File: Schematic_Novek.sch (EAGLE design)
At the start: 28 parts, among them IC1 STM32F10XCXT6, U1 BQ21040

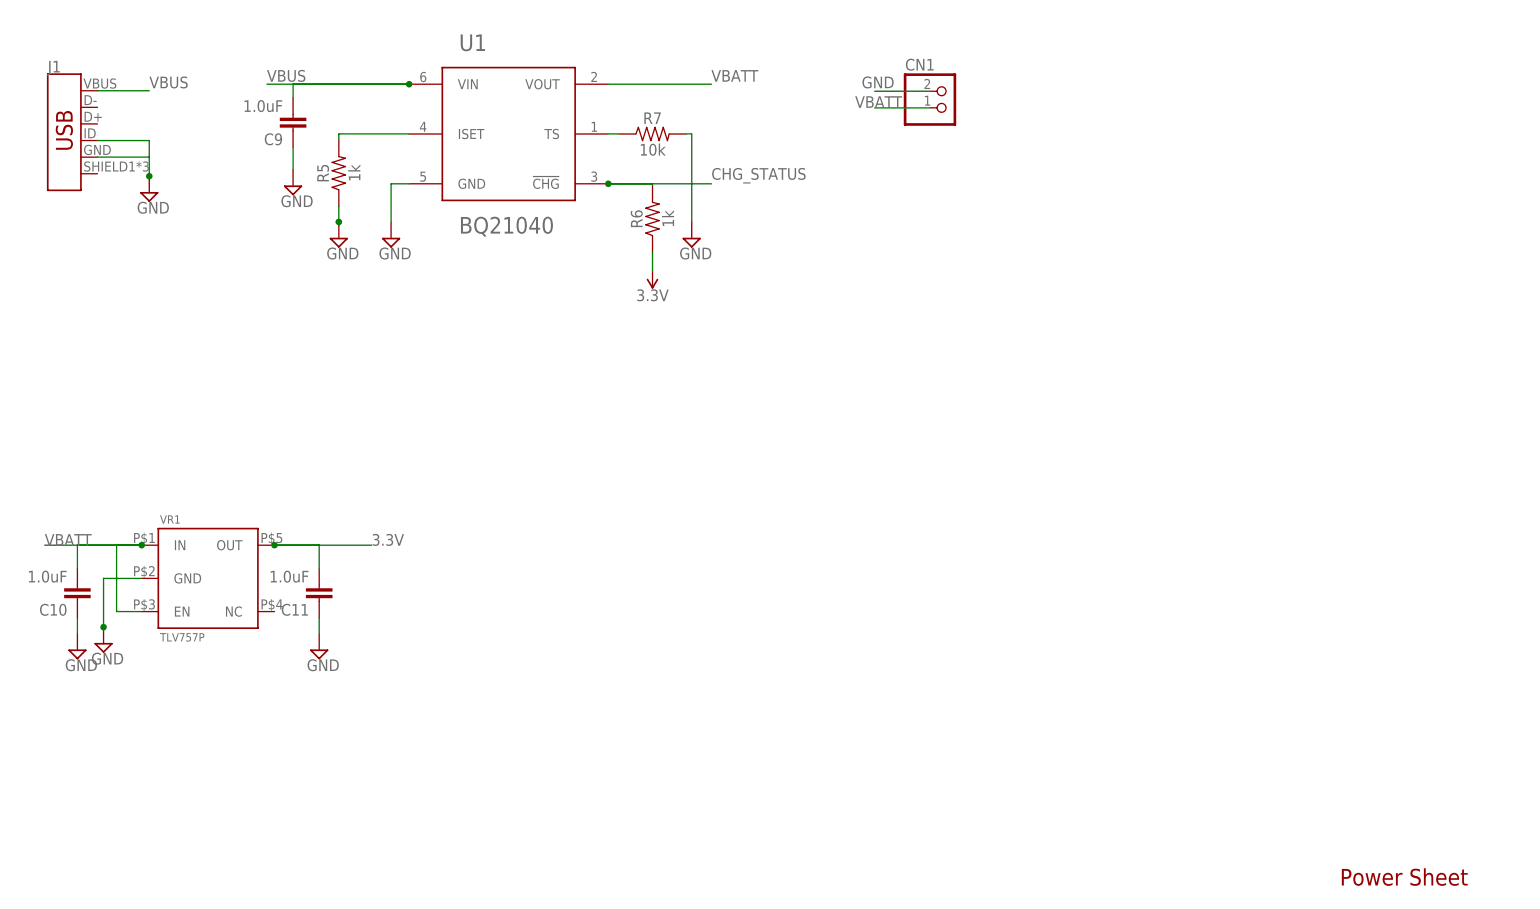
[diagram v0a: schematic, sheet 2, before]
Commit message: Adds max17048 fuel gauge
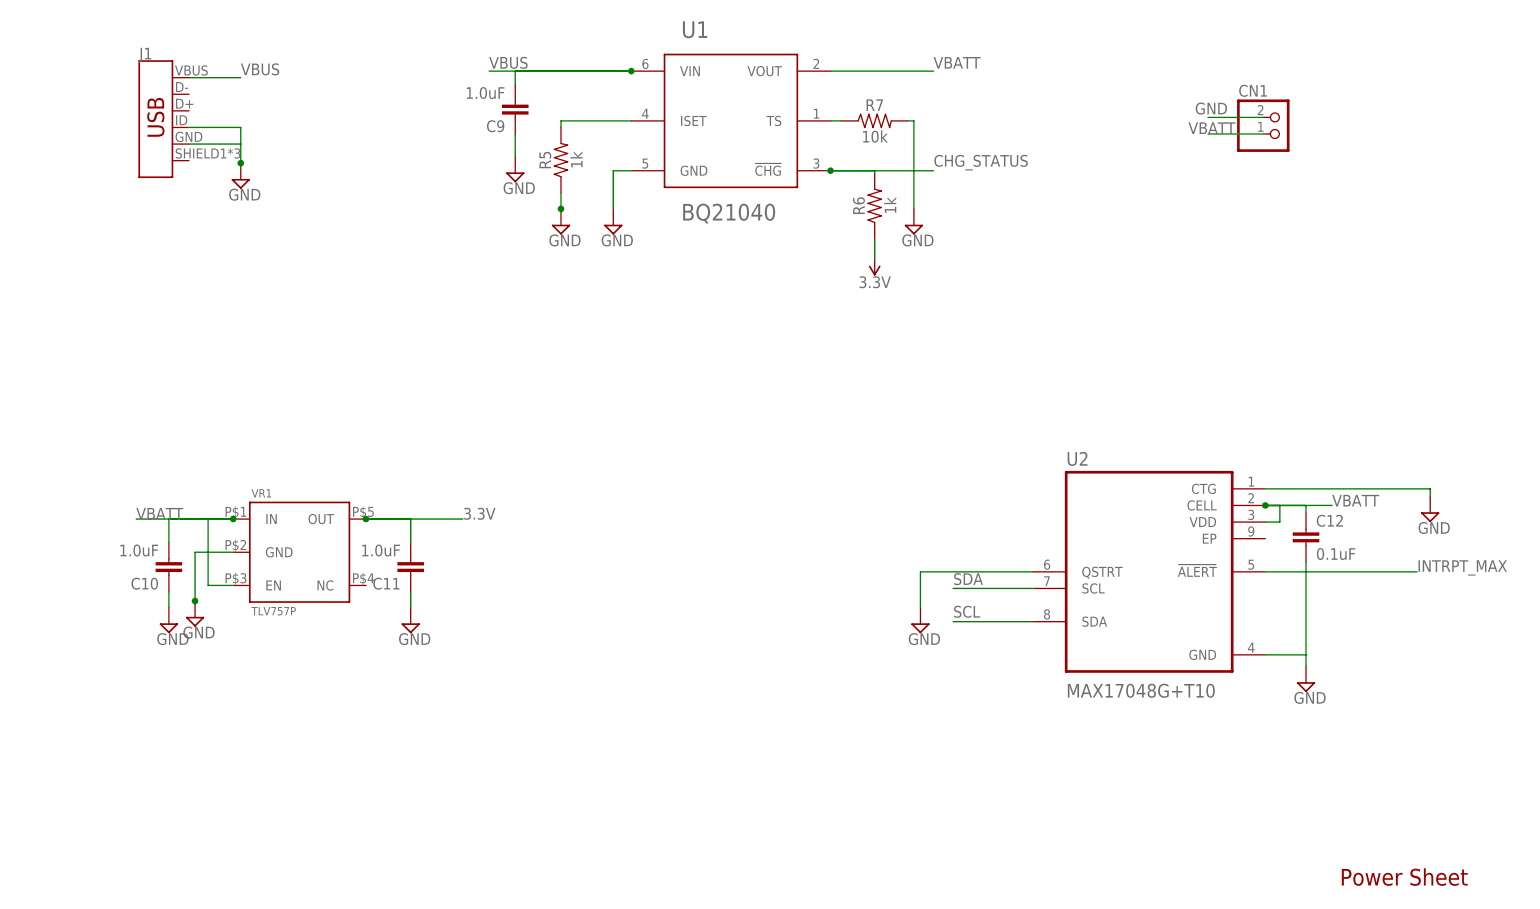
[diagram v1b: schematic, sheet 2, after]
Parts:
- added C12: 0.1uF, SparkFun-Capacitors:0.1UF-0603-25V-(+80/-20%)
- added U2: MAX17048G+T10, MAX17048G_T10:MAX17048G+T10
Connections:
- new net INTRPT_MAX: U2.!ALERT
- new net SCL: U2.SDA
- new net SDA: U2.SCL
- net GND: now also C12.2, U2.CTG, U2.GND, U2.QSTRT
- net VBATT: now also C12.1, U2.CELL, U2.VDD
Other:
- moved on the sheet: C10, C11, C9, CN1, J1, R5, R6, R7, U1, VR1

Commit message: Adds new sensor sheet
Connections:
- net CHG_STATUS: now also IC1PORTA_H.PA15
- net INTRPT_MAX: now also IC1PORTB_L.PB4
- net SCL: now also IC1PORTB_L.PB6
- net SDA: now also IC1PORTB_L.PB7
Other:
- note added: "Sensors + Transducers"
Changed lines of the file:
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@@
 <part name="SUPPLY25" library="supply2" deviceset="GND" device=""/>
 <part name="SUPPLY26" library="supply2" deviceset="GND" device=""/>
+<part name="FRAME3" library="frames" deviceset="A4L-LOC" device=""/>
 </parts>
 <sheets>
@@
 </segment>
 </net>
+<net name="SDA" class="0">
+<segment>
+<pinref part="IC1" gate="PORTB_L" pin="PB7"/>
+<wire x1="137.16" y1="114.3" x2="143" y2="114.3" width="0.1524" layer="91"/>
+<label x="143" y="115" size="1.778" layer="95"/>
+</segment>
+</net>
+<net name="SCL" class="0">
+<segment>
+<pinref part="IC1" gate="PORTB_L" pin="PB6"/>
+<wire x1="137.16" y1="116.84" x2="143" y2="116.84" width="0.1524" layer="91"/>
+<label x="143" y="117" size="1.778" layer="95"/>
+</segment>
+</net>
+<net name="INTRPT_MAX" class="0">
+<segment>
+<pinref part="IC1" gate="PORTB_L" pin="PB4"/>
+<wire x1="137.16" y1="121.92" x2="143" y2="121.92" width="0.1524" layer="91"/>
+<label x="143" y="122" size="1.778" layer="95"/>
+</segment>
+</net>
+<net name="CHG_STATUS" class="0">
+<segment>
+<pinref part="IC1" gate="PORTA_H" pin="PA15"/>
+<wire x1="101.6" y1="88.9" x2="91" y2="88.9" width="0.1524" layer="91"/>
+<label x="84" y="89" size="1.778" layer="95"/>
+</segment>
+</net>
 </nets>
 </sheet>
@@
 </nets>
 </sheet>
+<sheet>
+<plain>
+<text x="217.17" y="20" size="2.54" layer="94">Sensors + Transducers</text>
+</plain>
+<instances>
+<instance part="FRAME3" gate="G$1" x="0" y="0" smashed="yes">
+<attribute name="DRAWING_NAME" x="217.17" y="15.24" size="2.54" layer="94"/>
+<attribute name="LAST_DATE_TIME" x="217.17" y="10.16" size="2.286" layer="94"/>
+<attribute name="SHEET" x="230.505" y="5.08" size="2.54" layer="94"/>
+</instance>
+</instances>
+<busses>
+</busses>
+<nets>
+</nets>
+</sheet>

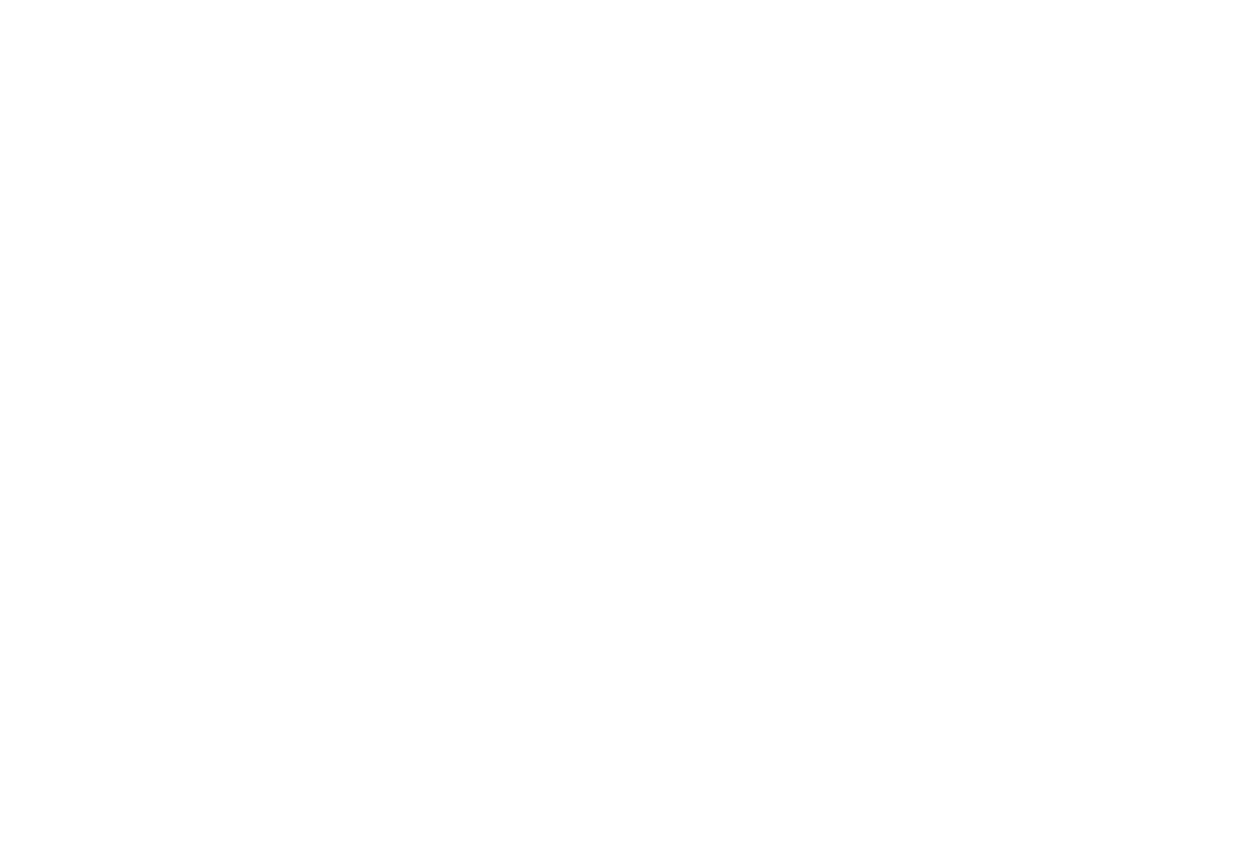
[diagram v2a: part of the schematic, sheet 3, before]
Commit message: Adds pressure gauge
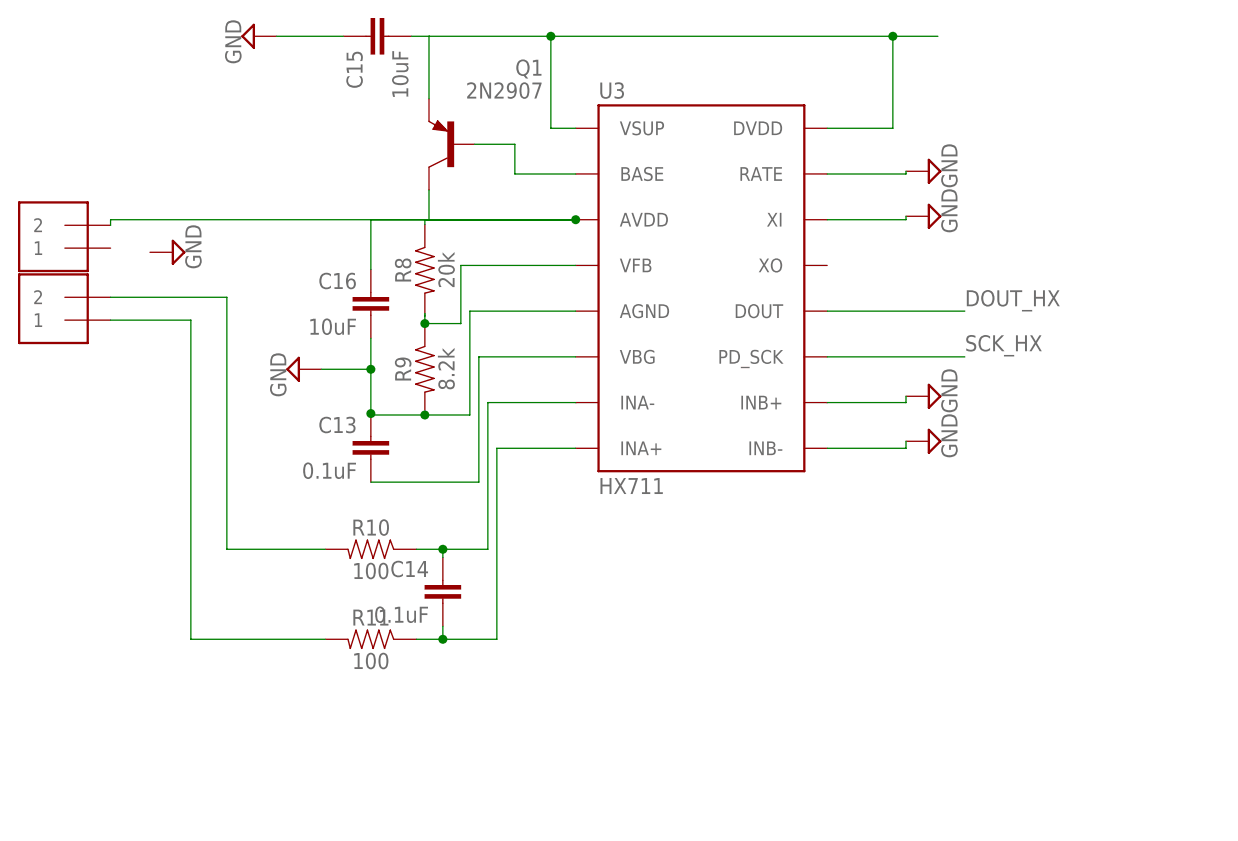
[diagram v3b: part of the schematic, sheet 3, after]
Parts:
- added C13, C14: 0.1uF, SparkFun-Capacitors:0.1UF-0603-25V-5%
- added C15, C16: 10uF, SparkFun-Capacitors:10UF-0603-6.3V-20%
- added J2, J3: 1X2-3.5MM, adafruit:1X2-3.5MM
- added Q1: 2N2907, adafruit:2N2907
- added R10, R11: 100, SparkFun-Resistors:100OHM-0603-1/10W-1%
- added R8: 20k, SparkFun-Resistors:20KOHM-0603-1/10W-1%
- added R9: 8.2k, SparkFun-Resistors:8.2KOHM-0603-1/10W-5%
- added U3: HX711, SparkFun-IC-Conversion:HX711
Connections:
- new net DOUT_HX: U3.DOUT
- new net N$10: C13.2, U3.VBG
- new net N$11: R8.2, R9.1, U3.VFB
- new net N$12: C14.1, R10.1, U3.INA-
- new net N$13: C14.2, R11.1, U3.INA+
- new net N$5: Q1.B, U3.BASE
- new net N$6: C15.2, Q1.E, U3.DVDD, U3.VSUP
- new net N$7: C16.1, J2.2, Q1.C, R8.1, U3.AVDD
- new net N$8: J3.2, R10.2
- new net N$9: J3.1, R11.2
- new net SCK_HX: U3.PD_SCK
- net GND: now also C13.1, C15.1, C16.2, R9.2, U3.AGND, U3.INB+, U3.INB-, U3.RATE, U3.XI

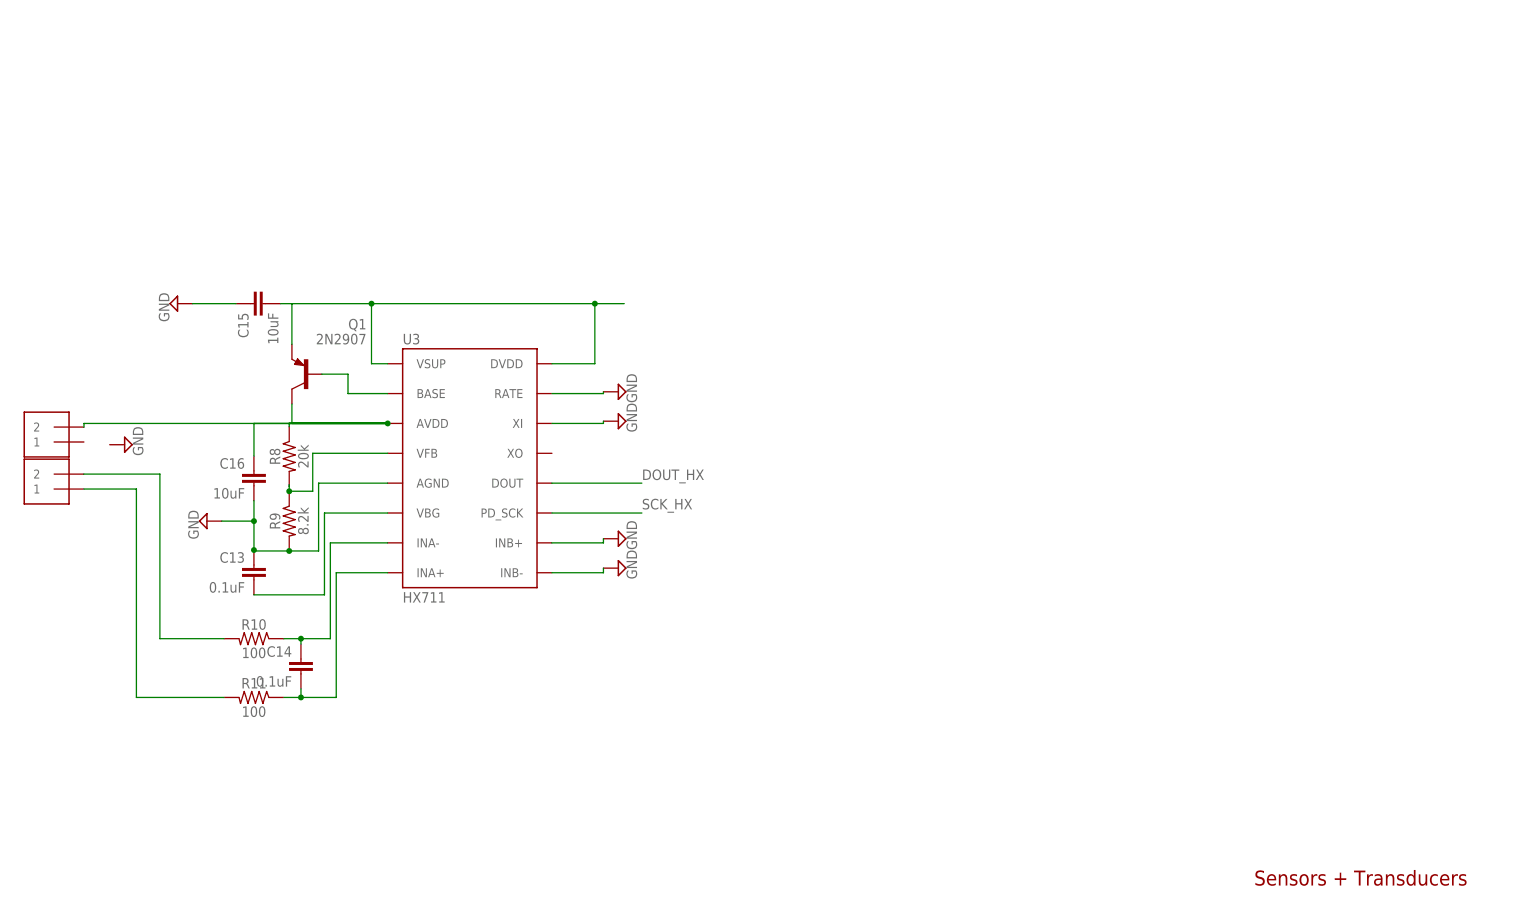
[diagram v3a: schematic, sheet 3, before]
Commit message: Adds sensor ports
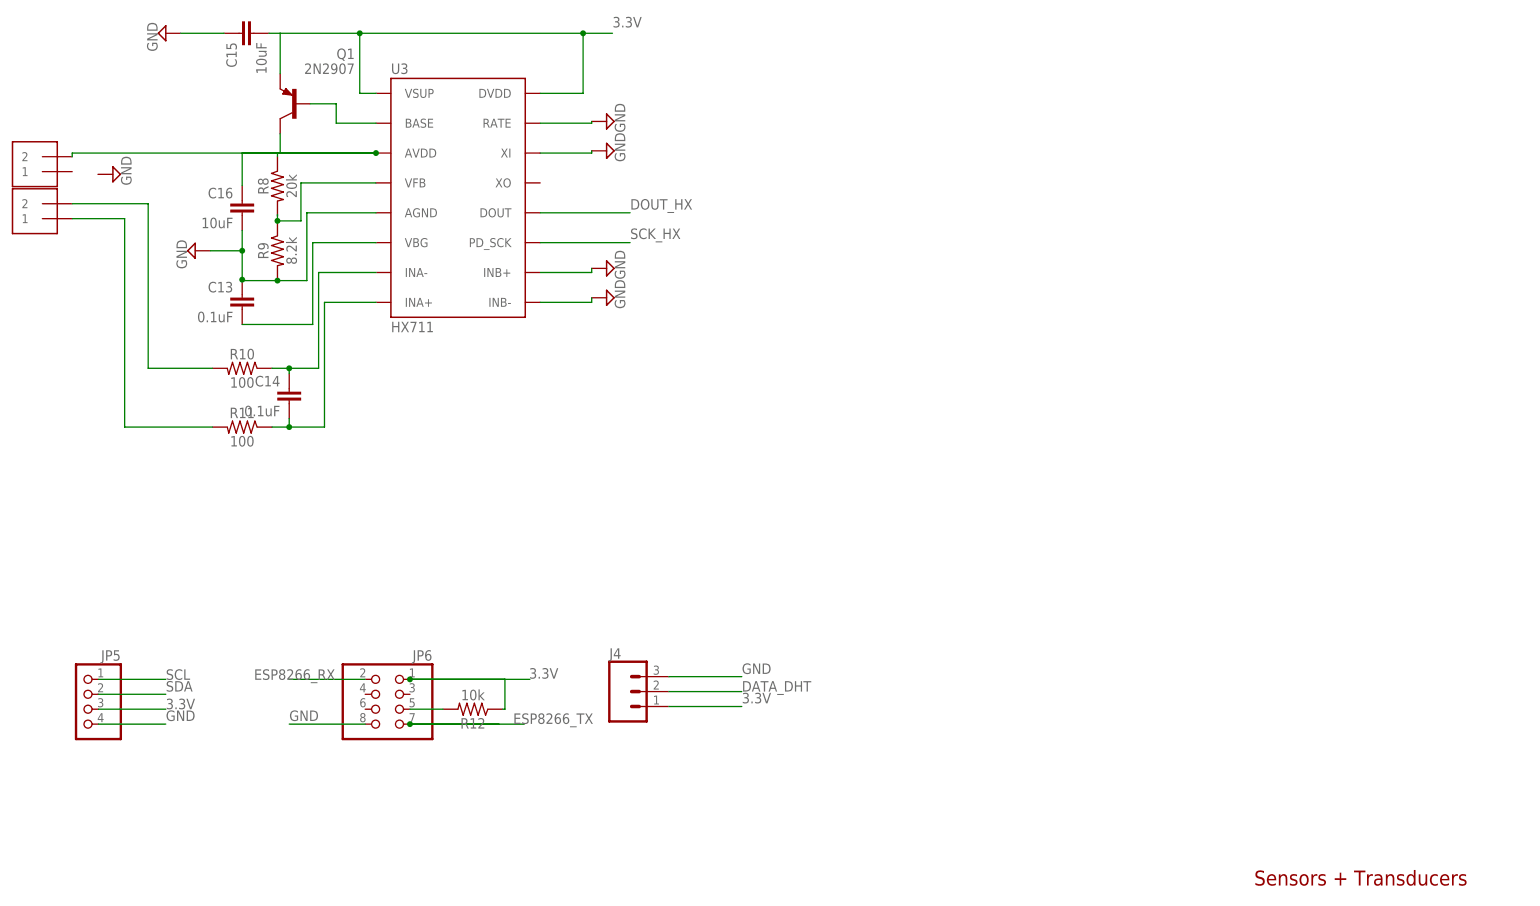
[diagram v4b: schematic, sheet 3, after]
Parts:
- added J4: (no value), SparkFun-Connectors:CONN_03JST-PTH
- added JP5: (no value), pinhead:PINHD-1X4
- added JP6: (no value), pinhead:PINHD-2X4
- added R12: 10k, SparkFun-Resistors:10KOHM-0603-1/10W-1%
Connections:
- new net DATA_DHT: IC1PORTA_L.PA7, J4.2
- new net ESP8266_RX: IC1PORTA_L.PA2, JP6.2
- new net ESP8266_TX: IC1PORTA_L.PA3, JP6.7
- net 3.3V: now also C15.2, J4.1, JP5.3, JP6.1, Q1.E, R12.1, U3.DVDD, U3.VSUP
- net DOUT_HX: now also IC1PORTA_L.PA4
- net GND: now also J4.3, JP5.4, JP6.8
- net N$6: now also JP6.5, R12.2; no longer C15.2, Q1.E, U3.DVDD, U3.VSUP
- net SCK_HX: now also IC1PORTA_L.PA5
- net SCL: now also JP5.1
- net SDA: now also JP5.2
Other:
- moved on the sheet: C13, C14, C15, C16, Q1, R10, R11, R8, R9, U3
